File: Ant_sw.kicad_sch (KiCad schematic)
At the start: 50 parts, among them J1 Conn_Coaxial, K2 G2R-1-E DC12, Q1 2N7002

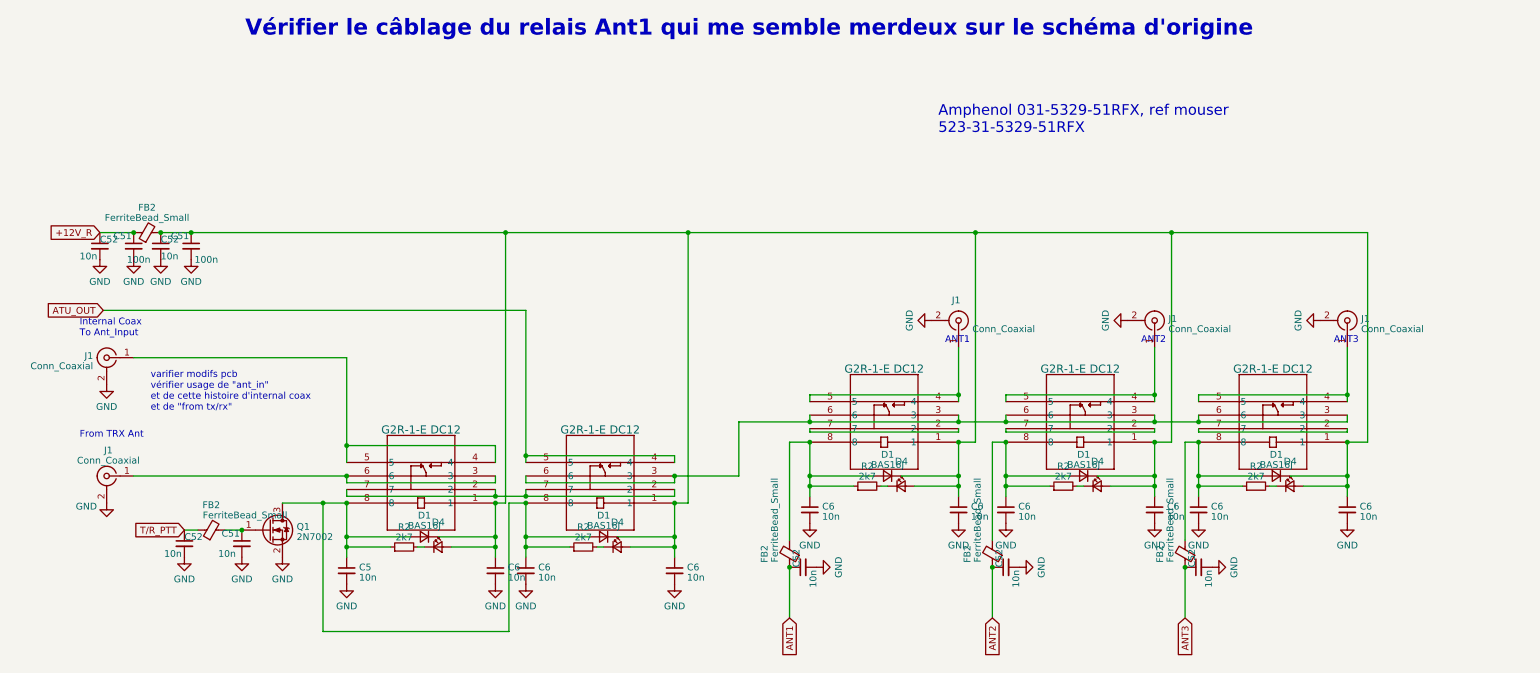
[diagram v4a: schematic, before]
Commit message: TRX relay back to G6A, minor changes
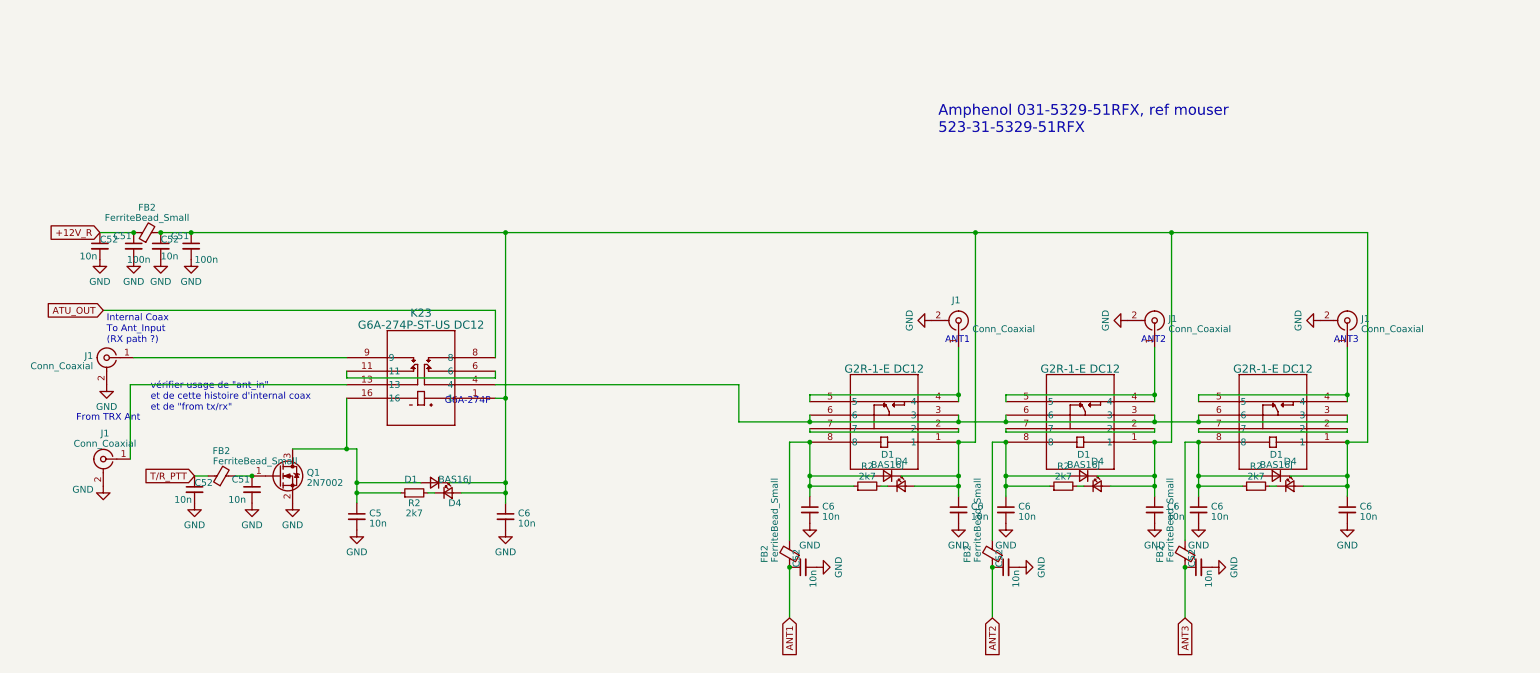
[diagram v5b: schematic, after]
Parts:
- removed C6 (x2): 10n, Capacitor_SMD:C_0805_2012Metric_Pad1.18x1.45mm_HandSolder, symbol Device:C_Small
- removed D1: BAS16J, Diode_SMD:D_SOD-323_HandSoldering, symbol Device:D_Small
- removed D4: LED_Small, LED_SMD:LED_1206_3216Metric_Pad1.42x1.75mm_HandSolder, symbol Device:LED_Small
- removed K2 (x2): G2R-1-E DC12, RELAY_G2R-1-E AC12:RELAY_G2R-1-E AC12, symbol RELAY_G2R-1-E AC12:G2R-1-E_DC12
- removed R2: 2k7, Resistor_SMD:R_0805_2012Metric_Pad1.20x1.40mm_HandSolder, symbol Device:R_Small
- added K23: G6A-274P-ST-US DC12, G6A-274P:G6A-274P, symbol G6A-274P:G6A-274P-ST-US_DC12
- J1: footprint BNC_Amphenol_031-5329-51RFX:BNC_Amphenol_031532951RFX -> SMA_PINS:SMA_PINS
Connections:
- net ATU_OUT: now also K23.8
- net at C51.1, C52.1, C6.1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: now also K23.1
- net at C5.1, D1.2 (A), Q1.3 (D)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: now also K23.16
- net at J1.1 (In): now also K23.9
- net at K2.3, K2.3, K2.3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: now also K23.4
- net at J1.1 (In): now also K23.13
- new net: K23.11, K23.6
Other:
- note added: "G6A-274P"
- note added: "Internal Coax To Ant_Input (RX path ?)"
- note added: "vérifier usage de "ant_in" et de cette histoire d'internal coax et de "from tx/rx""
- note removed: "Internal Coax To Ant_Input"
- note removed: "Vérifier le câblage du relais Ant1 qui me semble merdeux sur le schéma d'origine"
- note removed: "varifier modifs pcb vérifier usage de "ant_in" et de cette histoire d'internal coax et de "from tx/rx""
- moved on the sheet: C5, C51, C52, C6, D1, D4, FB2, J1, Q1, R2

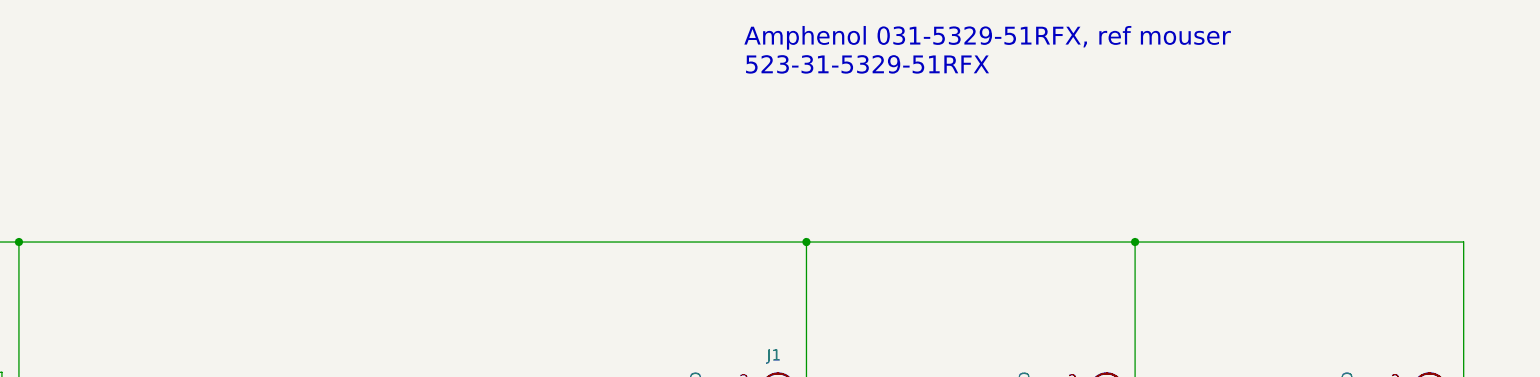
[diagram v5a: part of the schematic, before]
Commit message: placement F_Cu complete, starting B_Cu
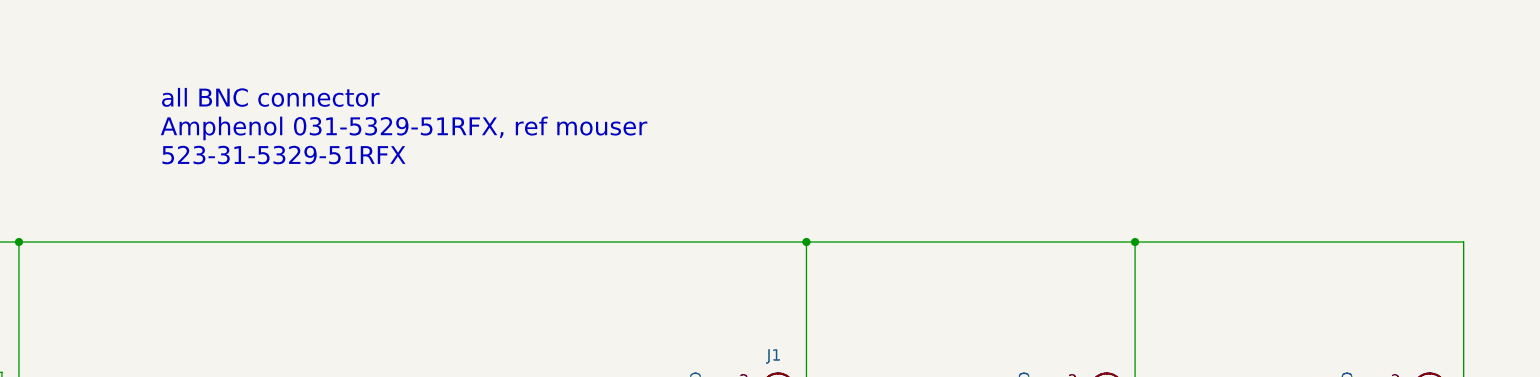
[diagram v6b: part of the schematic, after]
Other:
- note added: "all BNC connector Amphenol 031-5329-51RFX, ref mouser 523-31-5329-51RFX"
- note removed: "Amphenol 031-5329-51RFX, ref mouser 523-31-5329-51RFX"
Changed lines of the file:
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@@
     (effects (font (size 1.27 1.27)) (justify left bottom))
   )
-  (text "\nAmphenol 031-5329-51RFX, ref mouser \n523-31-5329-51RFX"
-    (at 180.34 60.325 0)
+  (text "all BNC connector\nAmphenol 031-5329-51RFX, ref mouser \n523-31-5329-51RFX"
+    (at 114.935 70.485 0)
     (effects (font (size 2 2)) (justify left bottom))
   )

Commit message: minor schematic mods
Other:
- note removed: "vérifier usage de "ant_in" et de cette histoire d'internal coax et de "from tx/rx""
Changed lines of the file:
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@@
-    (effects (font (size 1.27 1.27)) (justify left bottom))
-  )
-  (text "vérifier usage de \"ant_in\" \net de cette histoire d'internal coax\net de \"from tx/rx\"\n"
-    (at 32.385 112.395 0)
     (effects (font (size 1.27 1.27)) (justify left bottom))
   )

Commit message: more doc, silver mica bom
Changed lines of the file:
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@@
+    (stroke (width 0) (type default))
+  )
+  (wire (pts (xy 97.155 102.235) (xy 165.735 102.235))
     (stroke (width 0) (type default))
   )
@@
     (stroke (width 0) (type default))
   )
-  (wire (pts (xy 97.155 93.345) (xy 23.495 93.345))
-    (stroke (width 0) (type default))
-  )
   (wire (pts (xy 71.12 125.73) (xy 71.12 127.635))
     (stroke (width 0) (type default))
@@
   )
   (wire (pts (xy 156.21 109.22) (xy 184.15 109.22))
-    (stroke (width 0) (type default))
-  )
-  (wire (pts (xy 97.155 93.345) (xy 97.155 102.235))
     (stroke (width 0) (type default))
   )
@@
     )
   )
-  (global_label "ATU_OUT" (shape input) (at 23.495 93.345 180) (fields_autoplaced)
-    (effects (font (size 1.27 1.27)) (justify right))
-    (property "Intersheetrefs" "${INTERSHEET_REFS}" (at 12.6063 93.345 0)
-      (effects (font (size 1.27 1.27)) (justify right) hide)
+  (global_label "ATU_OUT" (shape input) (at 165.735 102.235 90) (fields_autoplaced)
+    (effects (font (size 1.27 1.27)) (justify left))
+    (property "Intersheetrefs" "${INTERSHEET_REFS}" (at 165.735 91.3463 90)
+      (effects (font (size 1.27 1.27)) (justify left) hide)
     )
   )
